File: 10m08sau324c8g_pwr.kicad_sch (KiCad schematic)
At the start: 49 parts

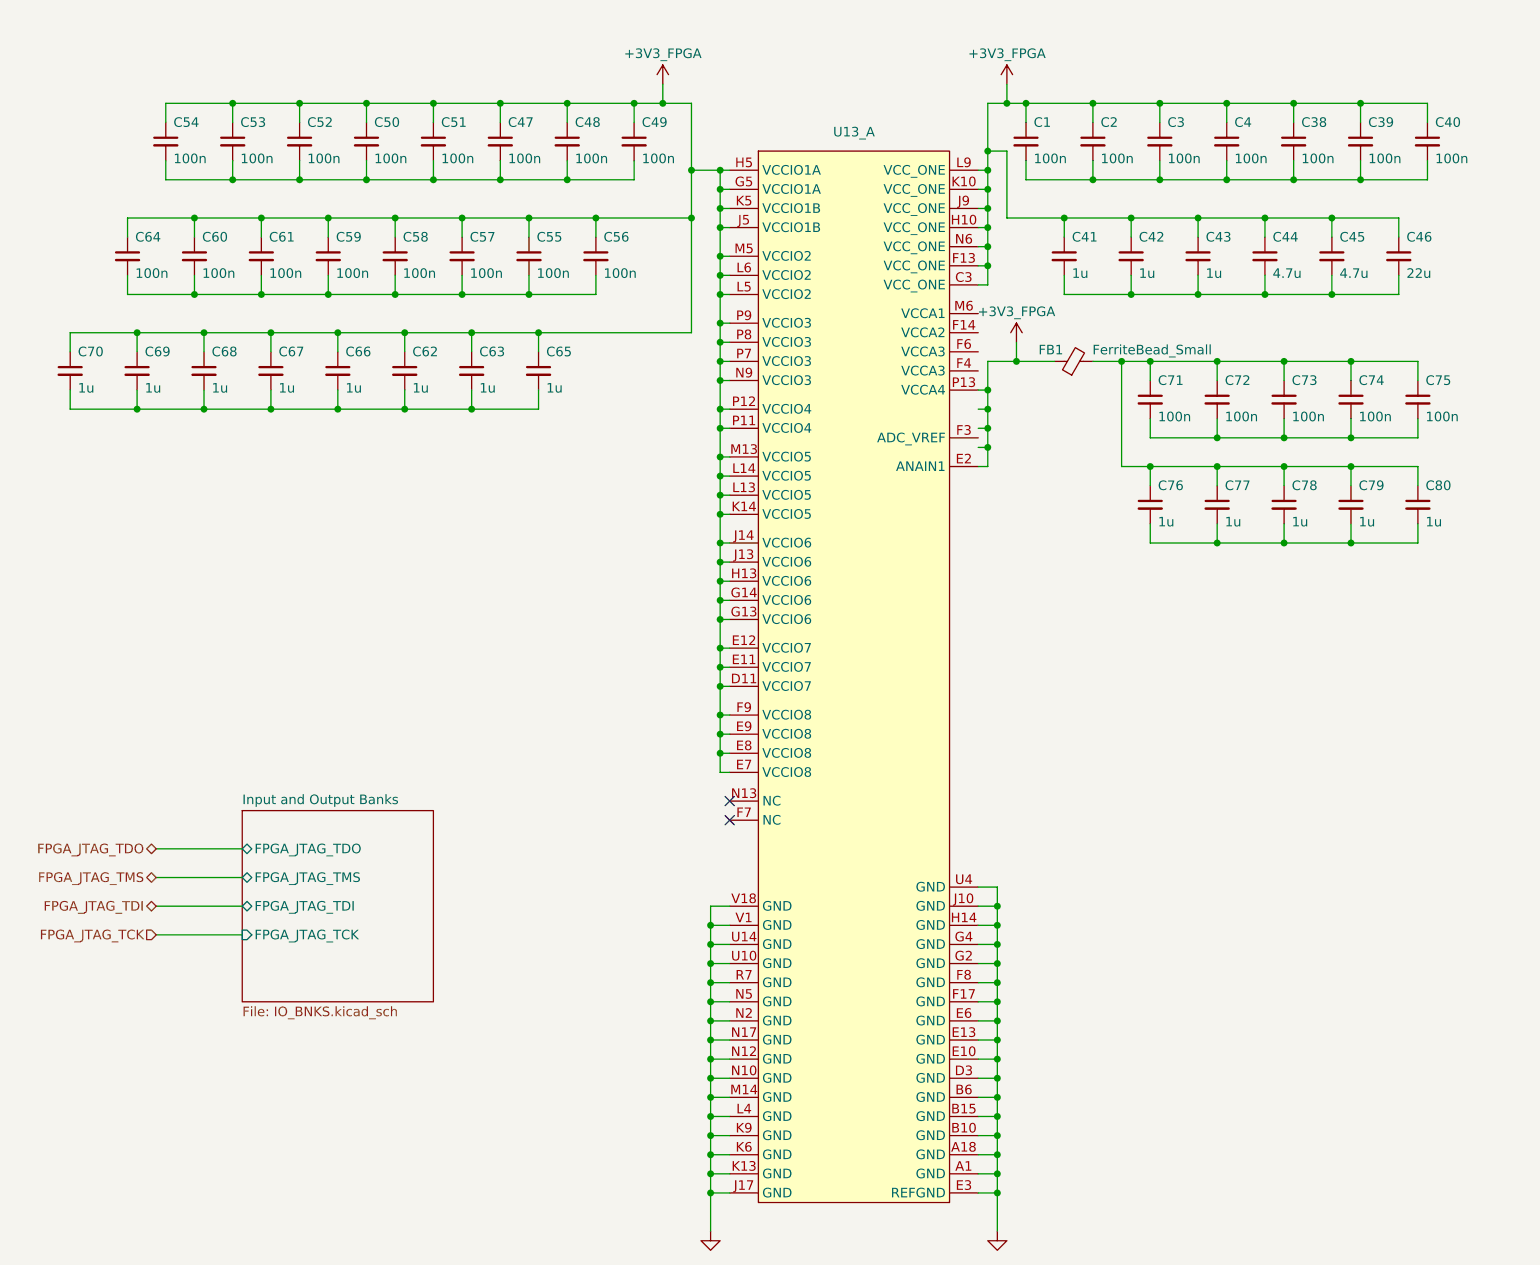
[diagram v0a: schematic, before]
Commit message: Hierarchy to flat
Attempting to convert the hierarchy type schematic into a flat one with the help of global labels
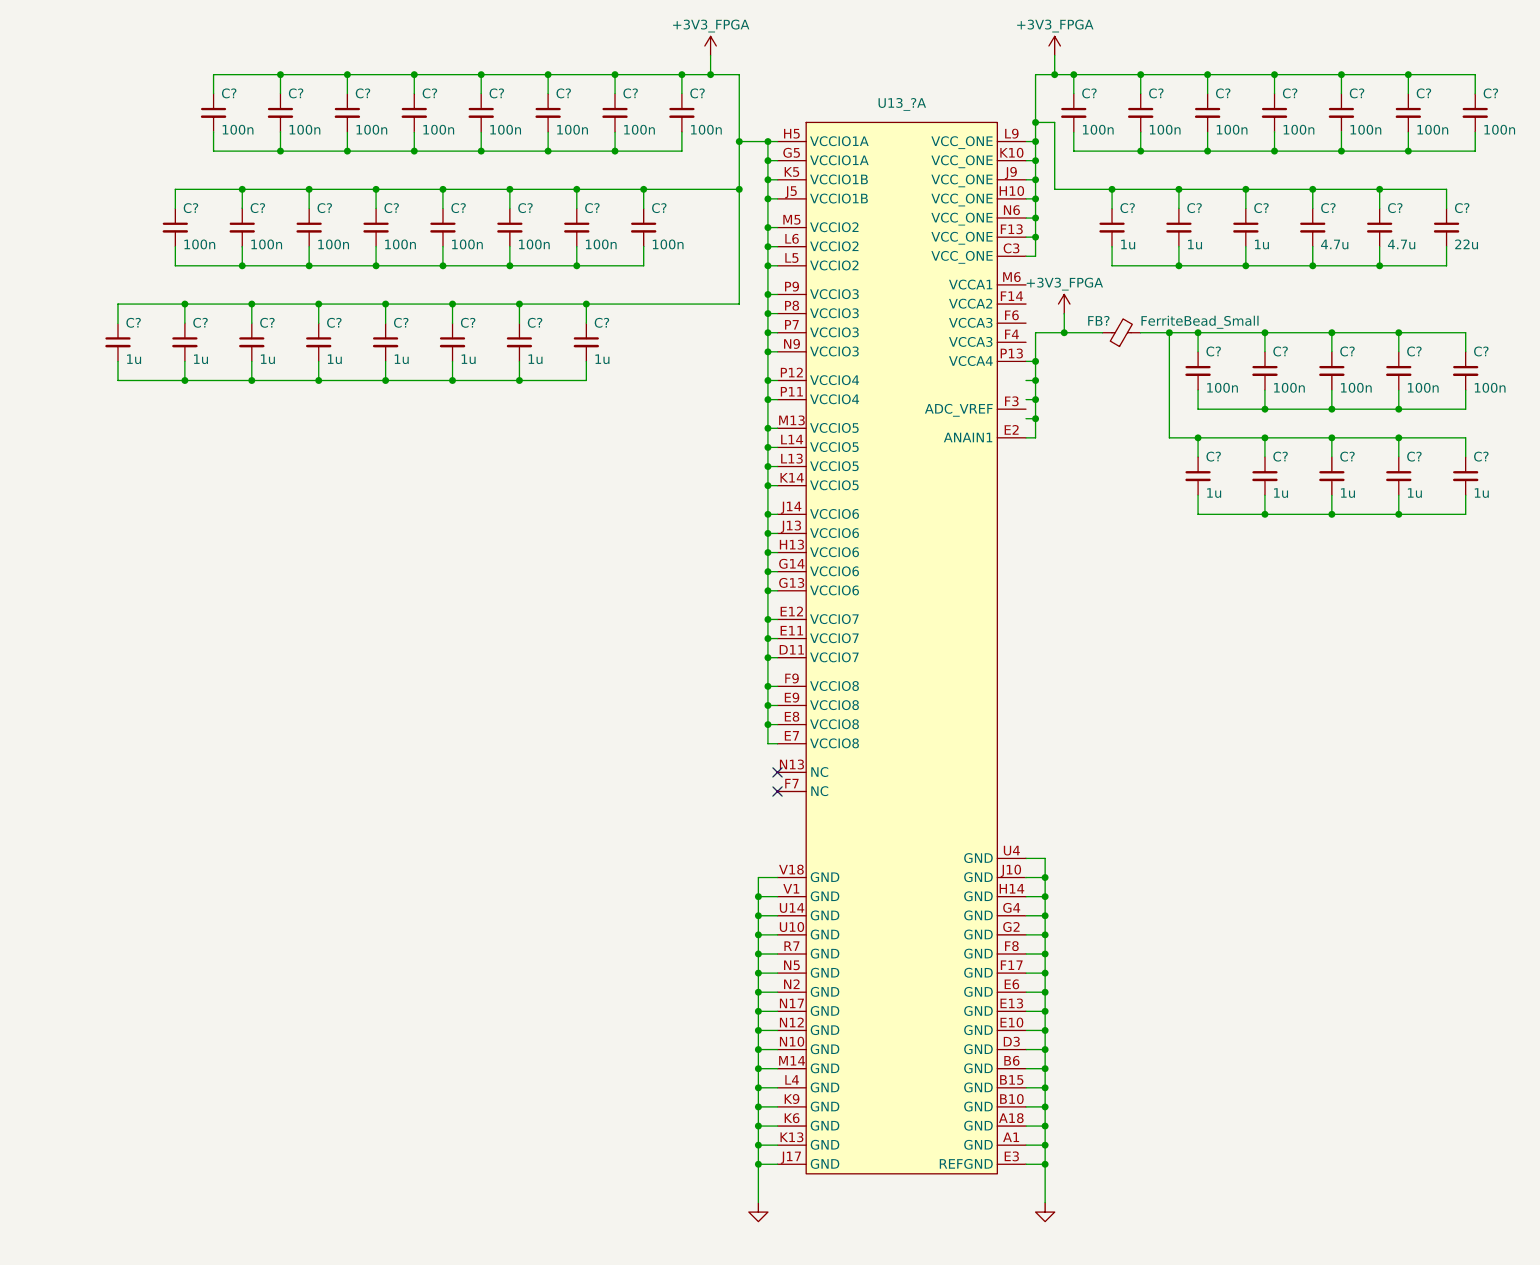
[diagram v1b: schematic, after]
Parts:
- removed C1, C2, C3, C38, C39, C4, C40, C47, C48, C49, C50, C51, C52, C53, C54, C55, C56, C57, C58, C59, C60, C61, C64, C71, C72, C73, C74, C75: 100n, symbol Device:C_Small
- removed C41, C42, C43, C62, C63, C65, C66, C67, C68, C69, C70, C76, C77, C78, C79, C80: 1u, symbol Device:C_Small
- removed C44, C45: 4.7u, symbol Device:C_Small
- removed C46: 22u, symbol Device:C_Small
- removed FB1: FerriteBead_Small, symbol Device:FerriteBead_Small
- removed U13_: (no value), 10M08SAU324C8G_FP:Untitled, symbol FPGA_Altera_Max10:10M08SAU324C8G
- added C? (x16): 1u, symbol Device:C_Small
- added C? (x28): 100n, symbol Device:C_Small
- added C? (x2): 4.7u, symbol Device:C_Small
- added C?: 22u, symbol Device:C_Small
- added FB?: FerriteBead_Small, symbol Device:FerriteBead_Small
- added U13_?: (no value), 10M08SAU324C8G_FP:Untitled, symbol FPGA_Altera_Max10:10M08SAU324C8G
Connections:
- net +3V3_FPGA: now also C?.1, C?.1, C?.1, C?.1, C?.1, C?.1, C?.1, C?.1, C?.1, C?.1, C?.1, C?.1, C?.1, C?.1, C?.1, C?.1, C?.1, C?.1, C?.1, C?.1, C?.1, C?.1, C?.1, C?.1, C?.1, C?.1, C?.1, C?.1, C?.1, C?.1, C?.1, C?.1, C?.1, C?.1, C?.1, C?.1, C?.1, FB?.1, U13_?.C3 (VCC_ONE), U13_?.D11 (VCCIO7), U13_?.E11 (VCCIO7), U13_?.E12 (VCCIO7), U13_?.E2 (ANAIN1), U13_?.E7 (VCCIO8), U13_?.E8 (VCCIO8), U13_?.E9 (VCCIO8), U13_?.F13 (VCC_ONE), U13_?.F9 (VCCIO8), U13_?.G13 (VCCIO6), U13_?.G14 (VCCIO6), U13_?.G5 (VCCIO1A), U13_?.H10 (VCC_ONE), U13_?.H13 (VCCIO6), U13_?.H5 (VCCIO1A), U13_?.J13 (VCCIO6), U13_?.J14 (VCCIO6), U13_?.J5 (VCCIO1B), U13_?.J9 (VCC_ONE), U13_?.K10 (VCC_ONE), U13_?.K14 (VCCIO5), U13_?.K5 (VCCIO1B), U13_?.L13 (VCCIO5), U13_?.L14 (VCCIO5), U13_?.L5 (VCCIO2), U13_?.L6 (VCCIO2), U13_?.L9 (VCC_ONE), U13_?.M13 (VCCIO5), U13_?.M5 (VCCIO2), U13_?.N6 (VCC_ONE), U13_?.N9 (VCCIO3), U13_?.P11 (VCCIO4), U13_?.P12 (VCCIO4), U13_?.P13 (VCCA4), U13_?.P7 (VCCIO3), U13_?.P8 (VCCIO3), U13_?.P9 (VCCIO3)
- net GND: now also U13_?.A1 (GND), U13_?.A18 (GND), U13_?.B10 (GND), U13_?.B15 (GND), U13_?.B6 (GND), U13_?.D3 (GND), U13_?.E10 (GND), U13_?.E13 (GND), U13_?.E3 (REFGND), U13_?.E6 (GND), U13_?.F17 (GND), U13_?.F8 (GND), U13_?.G2 (GND), U13_?.G4 (GND), U13_?.H14 (GND), U13_?.J10 (GND), U13_?.J17 (GND), U13_?.K13 (GND), U13_?.K6 (GND), U13_?.K9 (GND), U13_?.L4 (GND), U13_?.M14 (GND), U13_?.N10 (GND), U13_?.N12 (GND), U13_?.N17 (GND), U13_?.N2 (GND), U13_?.N5 (GND), U13_?.R7 (GND), U13_?.U10 (GND), U13_?.U14 (GND), U13_?.U4 (GND), U13_?.V1 (GND), U13_?.V18 (GND)
- new net: C?.2, C?.2, C?.2, C?.2, C?.2, C?.2, C?.2, C?.2 (x3)
- new net: C?.2, C?.2, C?.2, C?.2, C?.2, C?.2, C?.2
- new net: C?.2, C?.2, C?.2, C?.2, C?.2, C?.2
- new net: C?.1, C?.1, C?.1, C?.1, C?.1, C?.1, C?.1, C?.1, C?.1, C?.1, FB?.2
- new net: C?.2, C?.2, C?.2, C?.2, C?.2 (x2)
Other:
- removed sheet Input and Output Banks

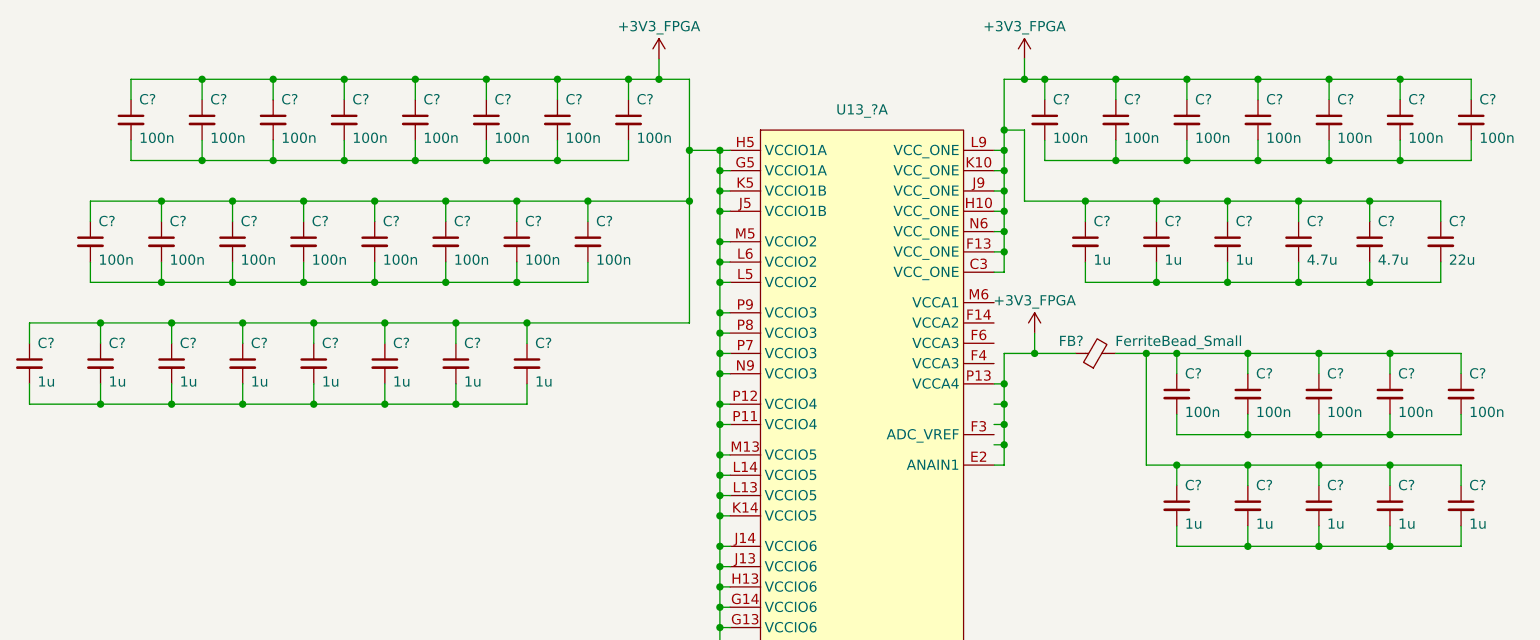
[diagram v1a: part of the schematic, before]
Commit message: Hierarchy to Flat completes
The hierarchy sheets have been converted into flat sheets and global labels have been used in appropriate place.
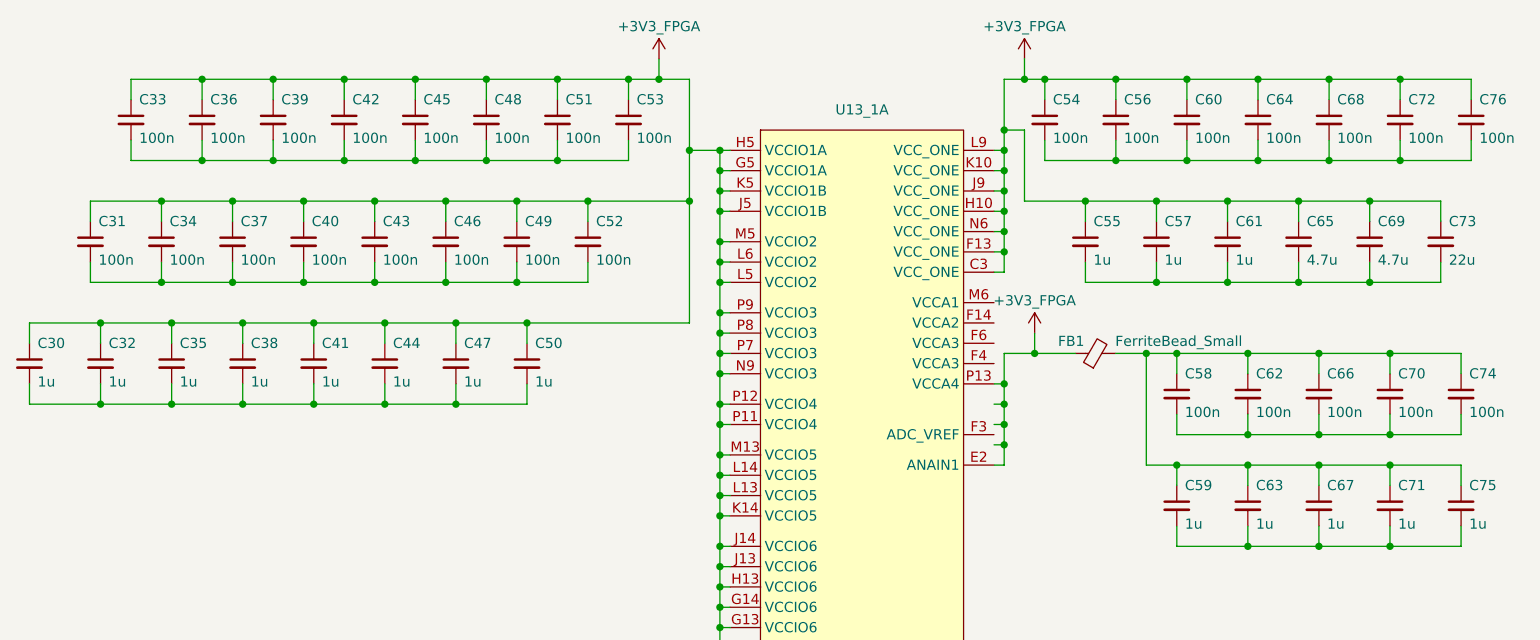
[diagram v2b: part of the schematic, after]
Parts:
- gave numbers to parts that had none: 49
